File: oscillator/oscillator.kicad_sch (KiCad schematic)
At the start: 24 parts, among them SW1 LFO Switch, U1 AS3340-custom, U2 TL074

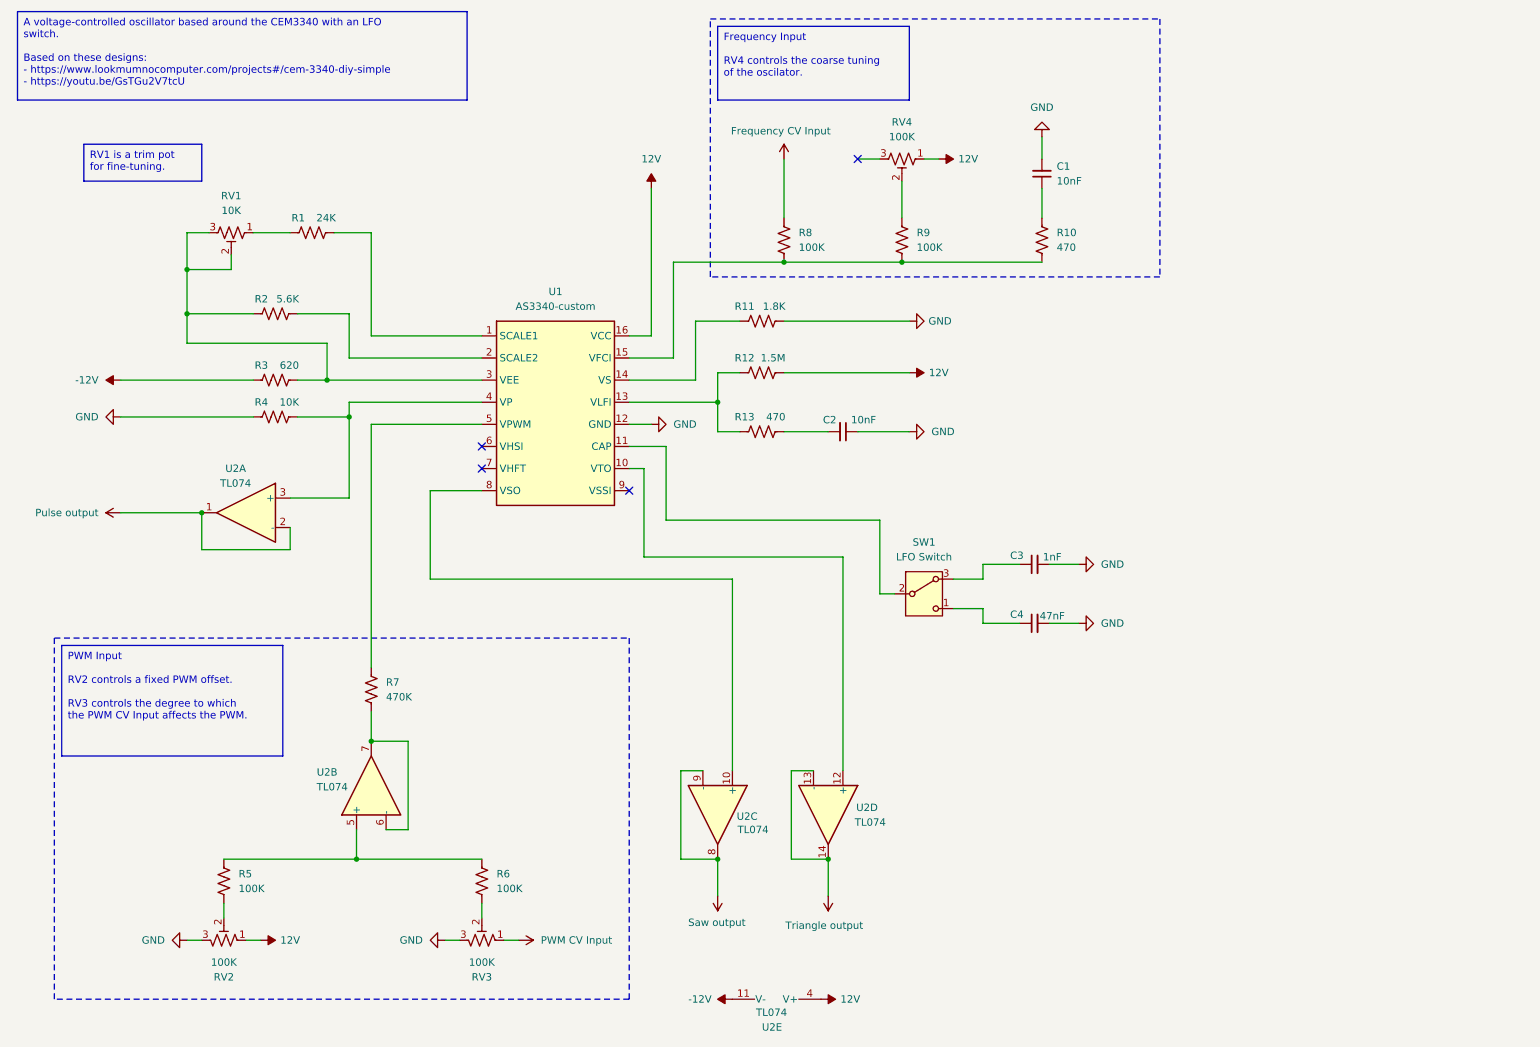
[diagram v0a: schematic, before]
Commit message: Add noise circuit to oscillator
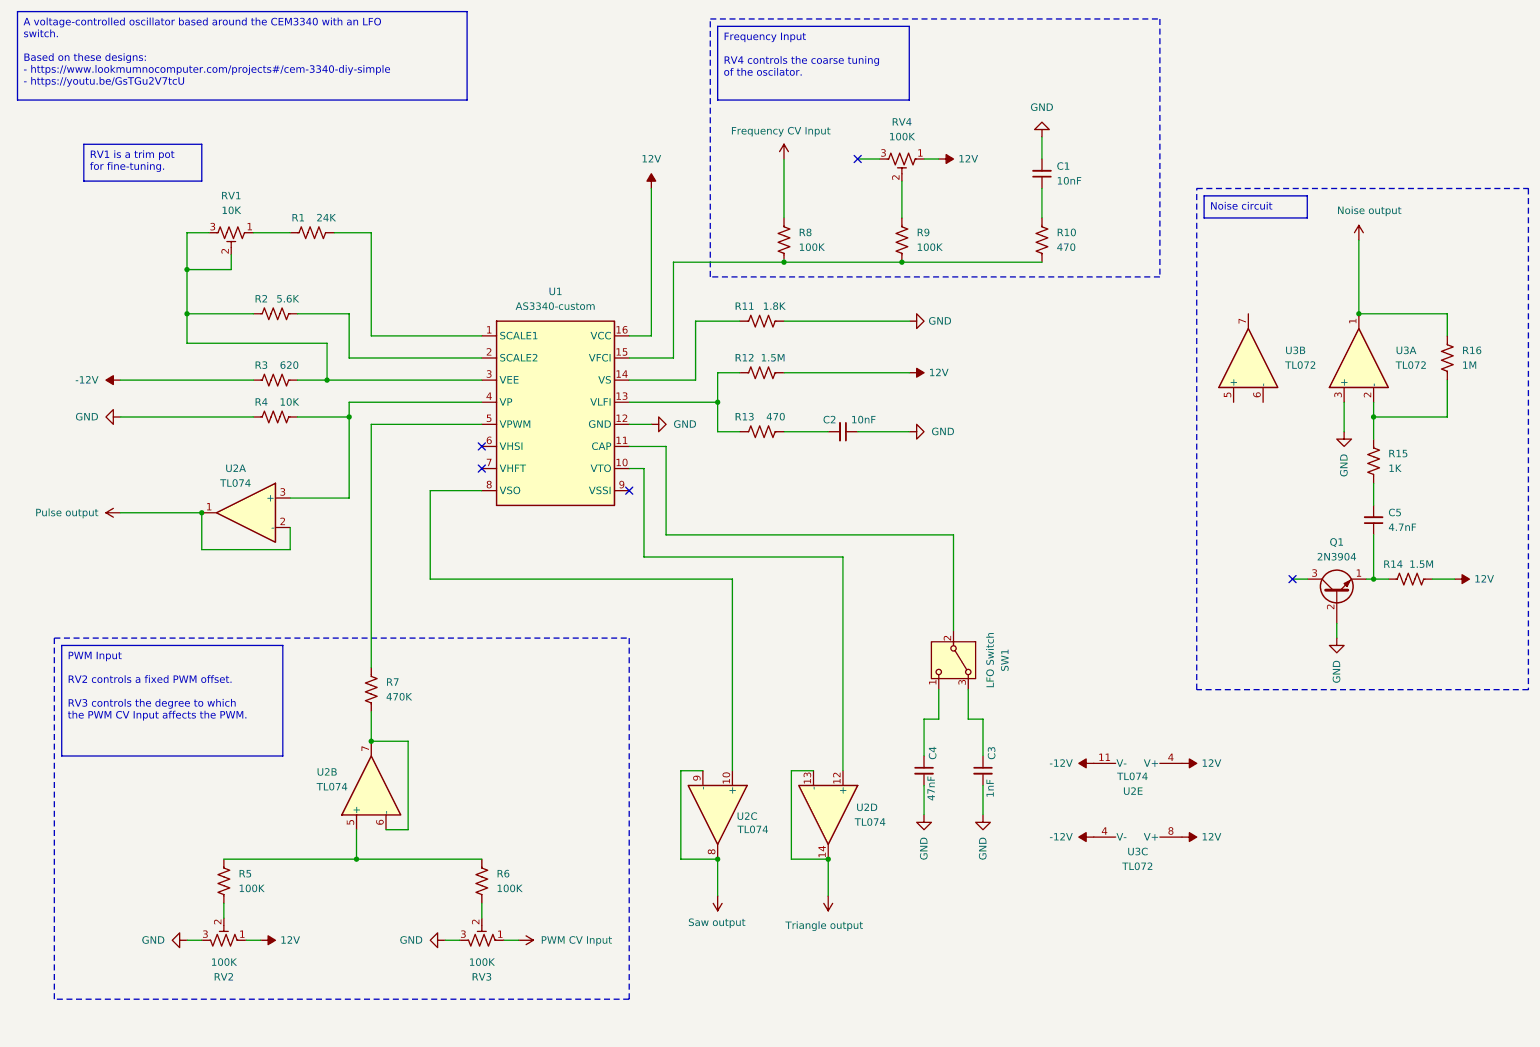
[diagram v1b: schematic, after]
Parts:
- added C5: 4.7nF, symbol Device:C_Small
- added Q1: 2N3904, Package_TO_SOT_THT:TO-92_Inline, symbol Transistor_BJT:2N3904
- added R14: 1.5M, symbol Device:R_US
- added R15: 1K, symbol Device:R_US
- added R16: 1M, symbol Device:R_US
- added U3: TL072, symbol Amplifier_Operational:TL072
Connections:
- net -12V: now also U3.4 (V-)
- net 12V: now also R14.2, U3.8 (V+)
- net GND: now also Q1.2 (B), U3.3 (+)
- new net: R15.1, R16.2, U3.2 (-)
- new net: C5.2, R15.2
- new net: C5.1, Q1.1 (E), R14.1
- new net Noise output: R16.1, U3.1
- no-connect marks 4 -> 5
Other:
- moved on the sheet: C3, C4, SW1, U2E

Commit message: Update oscillator schematic after building it
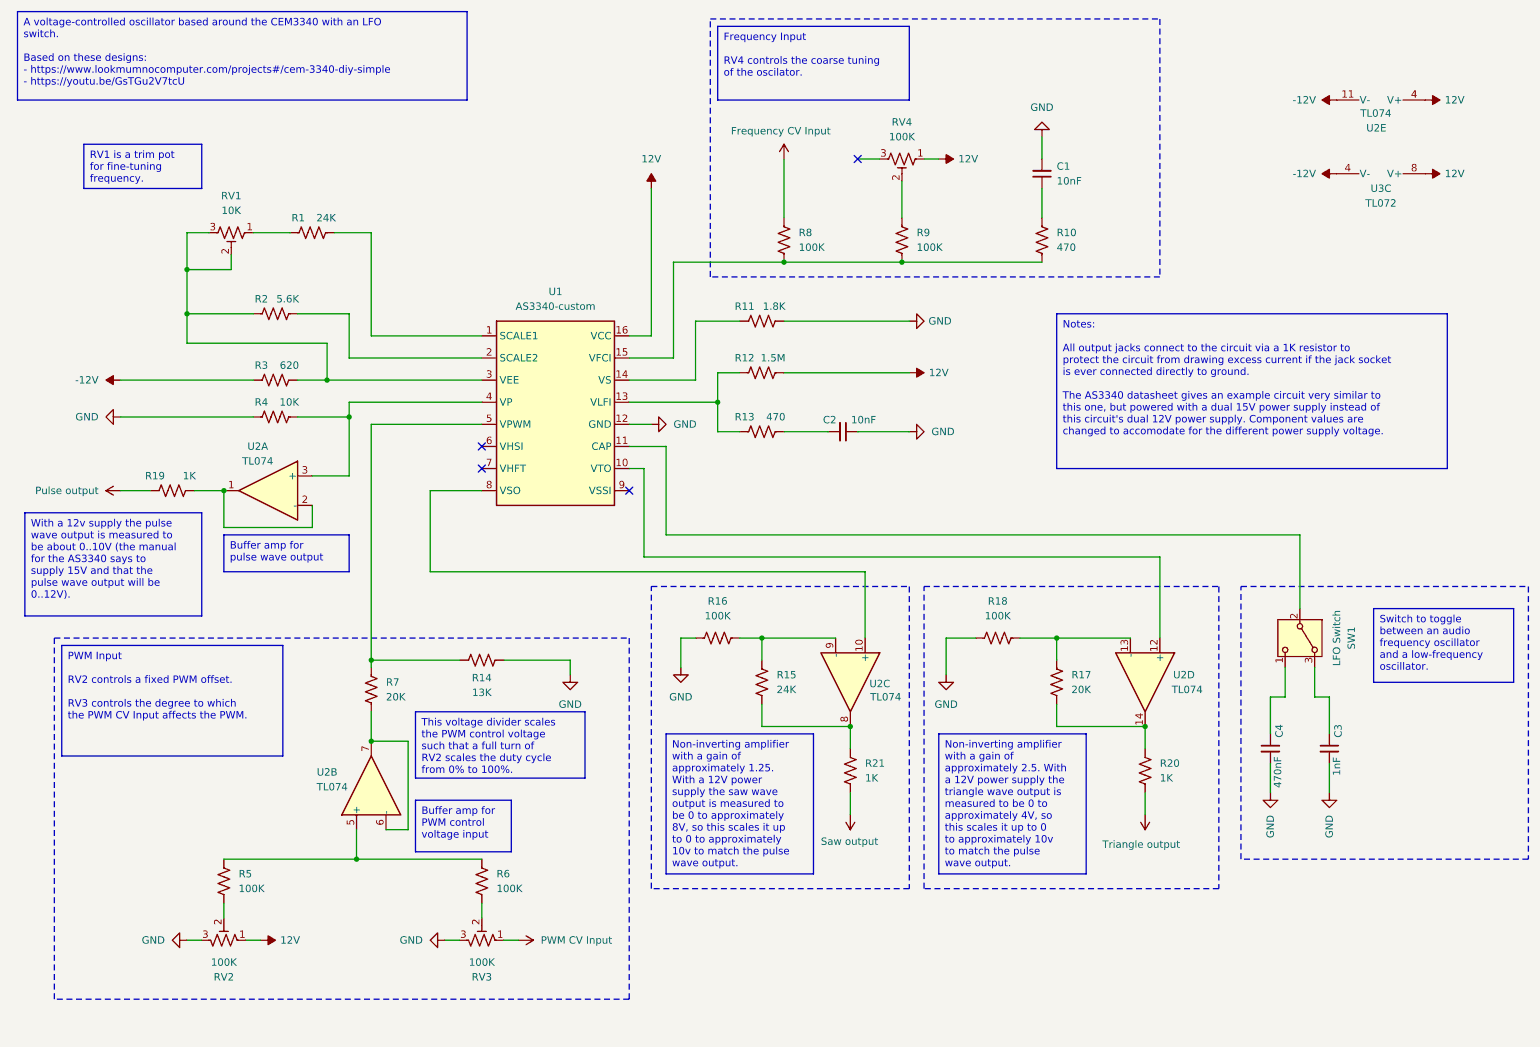
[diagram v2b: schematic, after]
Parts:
- removed C5: 4.7nF, symbol Device:C_Small
- removed Q1: 2N3904, Package_TO_SOT_THT:TO-92_Inline, symbol Transistor_BJT:2N3904
- removed unit 2 of U3
- removed unit 1 of U3
- added R17: 20K, symbol Device:R_US
- added R18: 100K, symbol Device:R_US
- added R19, R20, R21: 1K, symbol Device:R_US
- C4: value 47nF -> 470nF
- R14: value 1.5M -> 13K
- R15: value 1K -> 24K
- R16: value 1M -> 100K
- R7: value 470K -> 20K
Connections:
- net Noise output is gone; now on net GND: R16.1
- net 12V: no longer R14.2
- net GND: now also R14.2, R18.1
- net Pulse output: now also R19.1; no longer U2.1, U2.2 (-)
- net Saw output: now also R21.2; no longer U2.8, U2.9 (-)
- net Triangle output: now also R20.2; no longer U2.13 (-), U2.14
- net at R7.1, U1.5 (VPWM): now also R14.1
- net at R15.1, R16.2: now also U2.9 (-)
- net at R15.2: now also U2.8, R21.1
- new net: R17.2, R20.1, U2.14
- new net: R19.2, U2.1, U2.2 (-)
- new net: R17.1, R18.2, U2.13 (-)
- no-connect marks 5 -> 4
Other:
- moved on the sheet: C3, C4, SW1, U2A, U2C, U2D, U2E, U3C

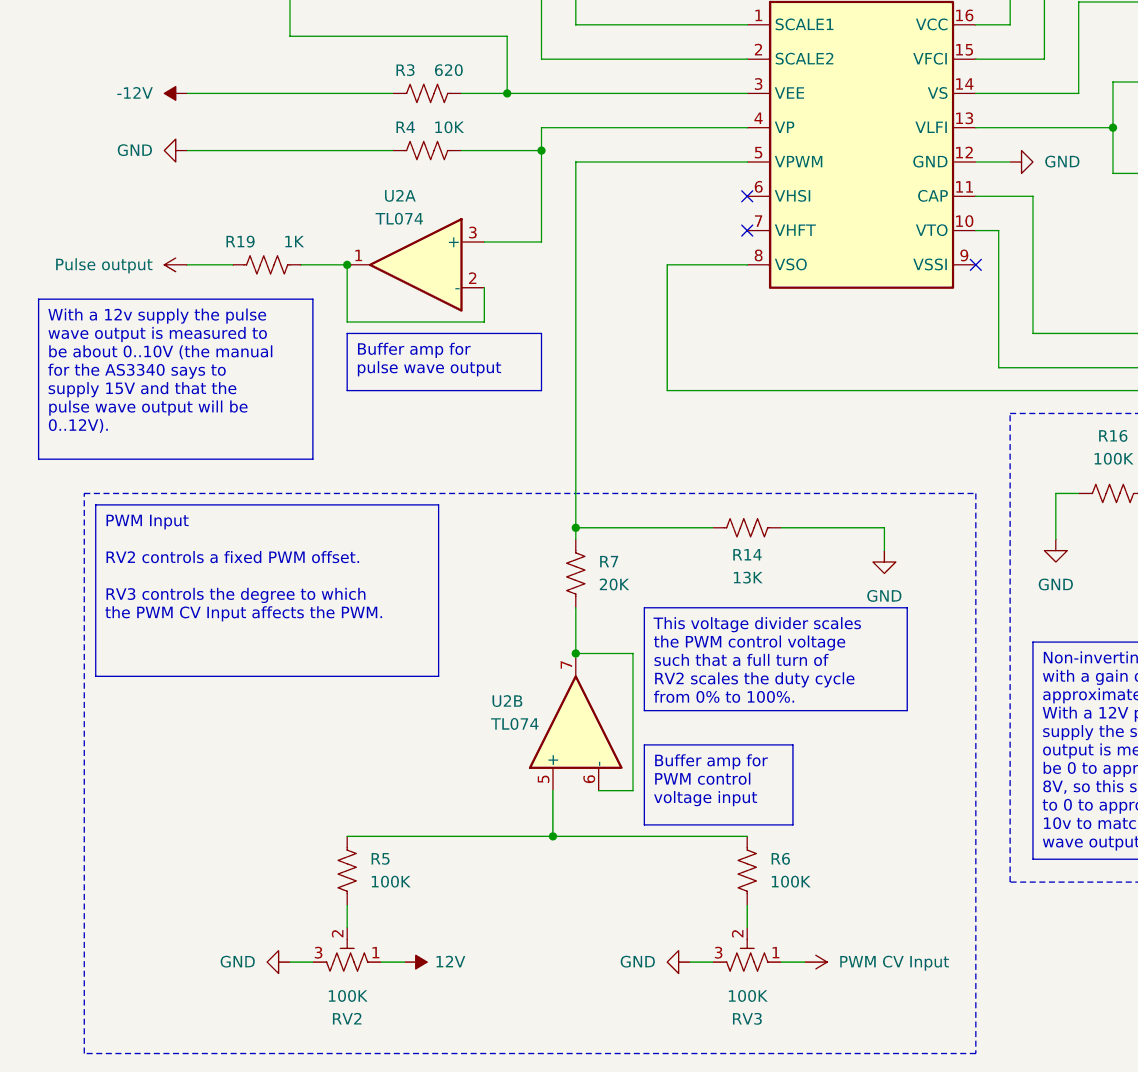
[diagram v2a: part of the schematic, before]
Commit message: Update oscillator
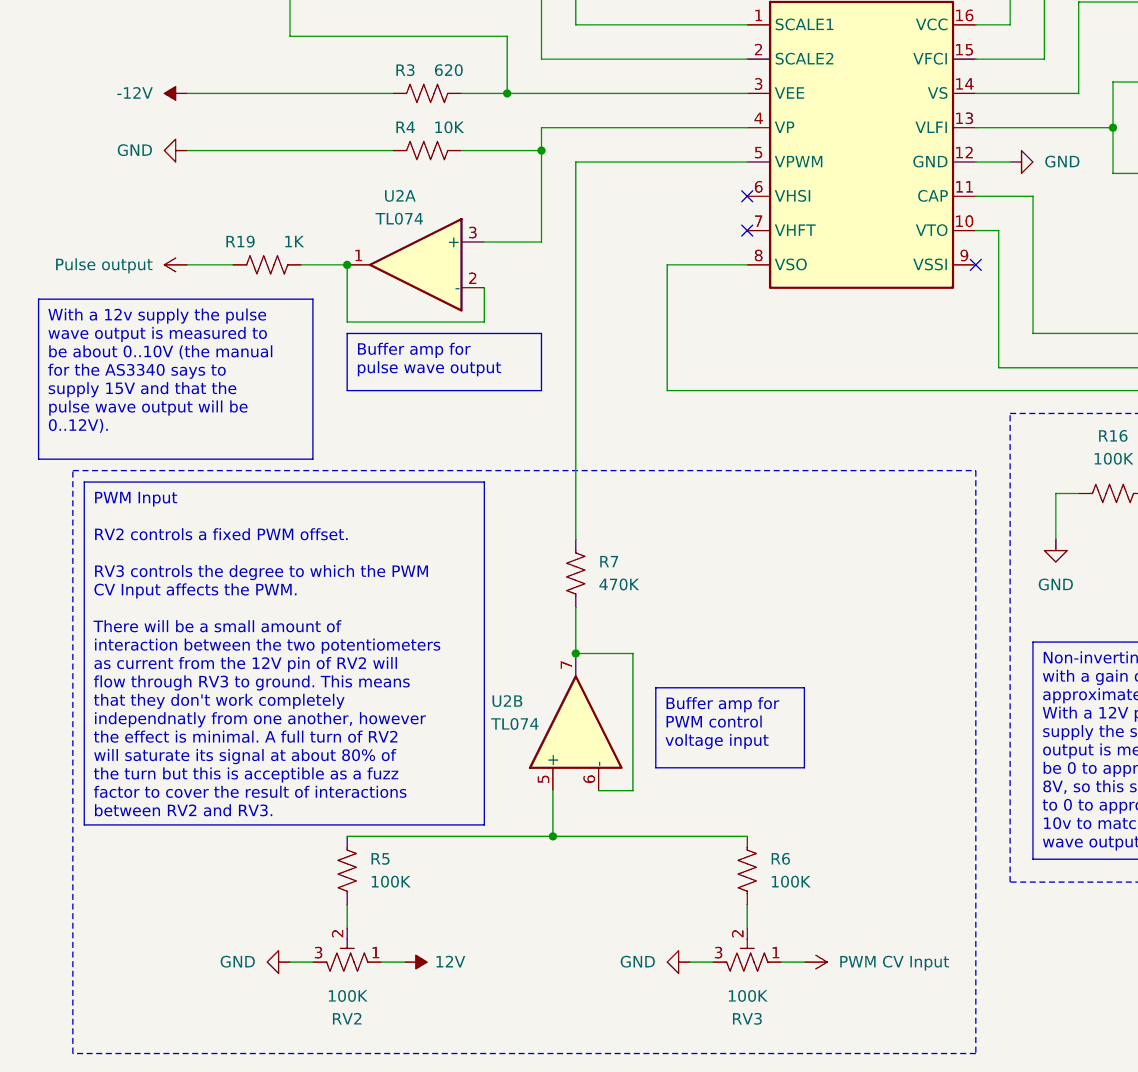
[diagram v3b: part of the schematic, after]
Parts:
- removed R14: 13K, symbol Device:R_US
- R7: value 20K -> 470K
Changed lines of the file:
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@@
-	)
-	(junction
-		(at 73.66 124.46)
-		(diameter 0)
-		(color 0 0 0 0)
 	)
 	(junction
@@
 	(wire
 		(pts
-			(xy 73.66 83.82) (xy 73.66 124.46)
-		)
-		(stroke
-			(width 0)
-			(type default)
-		)
-	)
-	(wire
-		(pts
 			(xy 191.77 135.89) (xy 191.77 132.08)
 		)
@@
 	(wire
 		(pts
-			(xy 73.66 124.46) (xy 73.66 125.73)
-		)
-		(stroke
-			(width 0)
-			(type default)
-		)
-	)
-	(wire
-		(pts
-			(xy 107.95 127) (xy 107.95 124.46)
+			(xy 73.66 83.82) (xy 73.66 125.73)
 		)
 		(stroke
@@
 	(wire
 		(pts
-			(xy 96.52 124.46) (xy 107.95 124.46)
-		)
-		(stroke
-			(width 0)
-			(type default)
-		)
-	)
-	(wire
-		(pts
 			(xy 30.48 82.55) (xy 53.34 82.55)
 		)
@@
 		)
 	)
-	(wire
-		(pts
-			(xy 73.66 124.46) (xy 88.9 124.46)
-		)
-		(stroke
-			(width 0)
-			(type default)
-		)
-	)
 	(rectangle
-		(start 19.05 120.65)
+		(start 17.78 118.11)
 		(end 118.11 182.88)
 		(stroke
@@
 		)
 	)
-	(text_box "This voltage divider scales the PWM control voltage such that a full turn of RV2 scales the duty cycle from 0% to 100%."
-		(exclude_from_sim no)
-		(at 81.28 133.35 0)
-		(size 29.21 11.43)
+	(text_box "PWM Input\n\nRV2 controls a fixed PWM offset.\n\nRV3 controls the degree to which the PWM CV Input affects the PWM.\n\nThere will be a small amount of interaction between the two potentiometers as current from the 12V pin of RV2 will flow through RV3 to ground. This means that they don't work completely independnatly from one another, however the effect is minimal. A full turn of RV2 will saturate its signal at about 80% of the turn but this is acceptible as a fuzz factor to cover the result of interactions between RV2 and RV3."
+		(exclude_from_sim no)
+		(at 19.05 119.38 0)
+		(size 44.45 38.1)
 		(stroke
 			(width 0)
@@
 		)
 	)
-	(text_box "PWM Input\n\nRV2 controls a fixed PWM offset.\n\nRV3 controls the degree to which the PWM CV Input affects the PWM."
-		(exclude_from_sim no)
-		(at 20.32 121.92 0)
-		(size 38.1 19.05)
+	(text_box "Switch to toggle between an audio frequency oscillator and a low-frequency oscillator."
+		(exclude_from_sim no)
+		(at 246.38 115.57 0)
+		(size 24.13 12.7)
 		(stroke
 			(width 0)
@@
 		)
 	)
-	(text_box "Switch to toggle between an audio frequency oscillator and a low-frequency oscillator."
-		(exclude_from_sim no)
-		(at 246.38 115.57 0)
-		(size 24.13 12.7)
-		(stroke
-			(width 0)
-			(type default)
-		)
-		(fill
-			(type none)
-		)
-		(effects
-			(font
-				(size 1.27 1.27)
-			)
-			(justify left top)
-		)
-	)
 	(text_box "Buffer amp for PWM control voltage input"
 		(exclude_from_sim no)
-		(at 81.28 148.59 0)
+		(at 82.55 142.24 0)
 		(size 16.51 8.89)
 		(stroke
@@
 	(symbol
 		(lib_id "Device:R_US")
-		(at 92.71 124.46 90)
-		(unit 1)
-		(exclude_from_sim no)
-		(in_bom yes)
-		(on_board yes)
-		(dnp no)
-		(property "Reference" "R14"
-			(at 92.71 127.508 90)
-			(effects
-				(font
-					(size 1.27 1.27)
-				)
-			)
-		)
-		(property "Value" "13K"
-			(at 92.71 130.048 90)
-			(effects
-				(font
-					(size 1.27 1.27)
-				)
-			)
-		)
-		(property "Footprint" ""
-			(at 92.964 123.444 90)
-			(effects
-				(font
-					(size 1.27 1.27)
-				)
-				(hide yes)
-			)
-		)
-		(property "Datasheet" "~"
-			(at 92.71 124.46 0)
-			(effects
-				(font
-					(size 1.27 1.27)
-				)
-				(hide yes)
-			)
-		)
-		(property "Description" "Resistor, US symbol"
-			(at 92.71 124.46 0)
-			(effects
-				(font
-					(size 1.27 1.27)
-				)
-				(hide yes)
-			)
-		)
-		(pin "2"
-		)
-		(pin "1"
-		)
-		(instances
-			(project "oscillator"
-				(path "/7dd35790-78ae-4a1f-bde7-c41292af2ddc"
-					(reference "R14")
-					(unit 1)
-				)
-			)
-		)
-	)
-	(symbol
-		(lib_id "Device:R_US")
 		(at 73.66 129.54 0)
 		(unit 1)
@@
 			)
 		)
-		(property "Value" "20K"
+		(property "Value" "470K"
 			(at 76.2 130.8099 0)
 			(effects
@@
 					(unit 1)
 				)
-			)
-		)
-	)
-	(symbol
-		(lib_id "power:GND")
-		(at 107.95 127 0)
-		(unit 1)
-		(exclude_from_sim no)
-		(in_bom yes)
-		(on_board yes)
-		(dnp no)
-		(fields_autoplaced yes)
-		(property "Reference" "#PWR022"
-			(at 107.95 133.35 0)
-			(effects
-				(font
-					(size 1.27 1.27)
-				)
-				(hide yes)
-			)
-		)
-		(property "Value" "GND"
-			(at 107.95 132.08 0)
-			(effects
-				(font
-					(size 1.27 1.27)
-				)
-			)
-		)
-		(property "Footprint" ""
-			(at 107.95 127 0)
-			(effects
-				(font
-					(size 1.27 1.27)
-				)
-				(hide yes)
-			)
-		)
-		(property "Datasheet" ""
-			(at 107.95 127 0)
-			(effects
-				(font
-					(size 1.27 1.27)
-				)
-				(hide yes)
-			)
-		)
-		(property "Description" "Power symbol creates a global label with name \"GND\" , ground"
-			(at 107.95 127 0)
-			(effects
-				(font
-					(size 1.27 1.27)
-				)
-				(hide yes)
-			)
-		)
-		(pin "1"
-		)
-		(instances
-			(project "oscillator"
-				(path "/7dd35790-78ae-4a1f-bde7-c41292af2ddc"
-					(reference "#PWR022")
-					(unit 1)
-				)
